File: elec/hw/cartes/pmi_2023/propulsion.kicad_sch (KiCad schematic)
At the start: 45 parts, among them Q1 SI2310, U1 DRV8231ADDAR, U2 DRV8231ADDAR, U3 EESX1321, U4 EESX1321

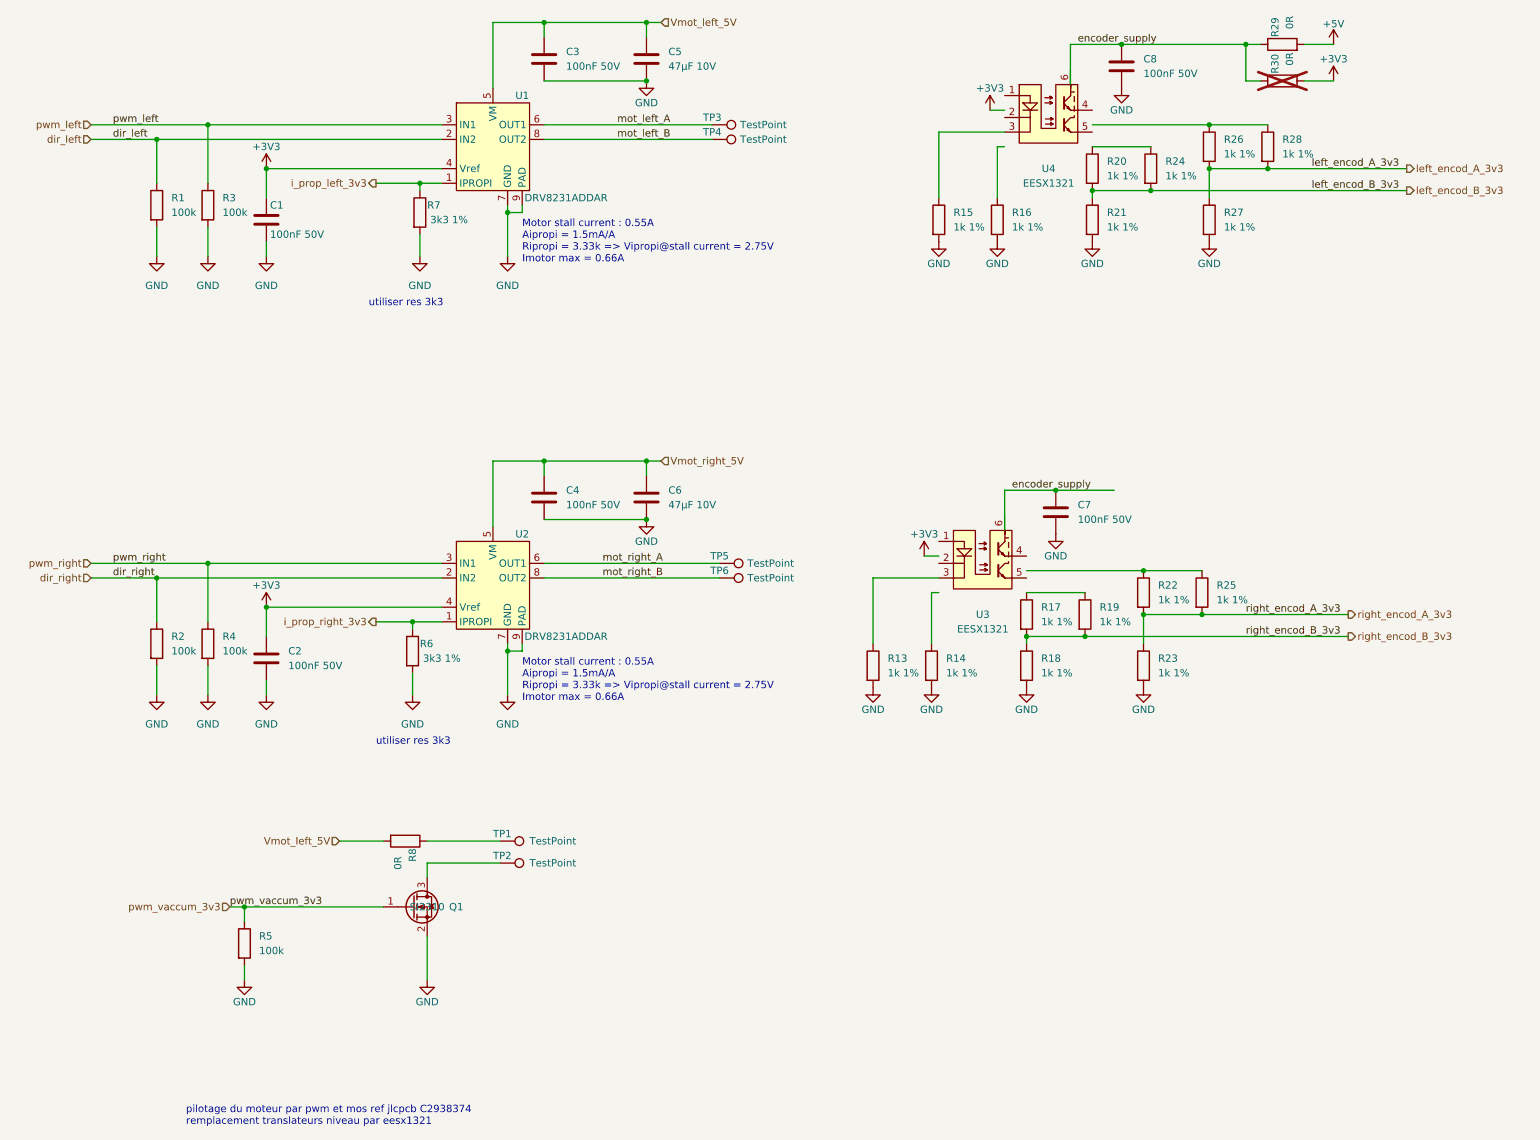
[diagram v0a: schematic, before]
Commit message: reset button added to esp32 reset. uart prog connector replaces ftdi one
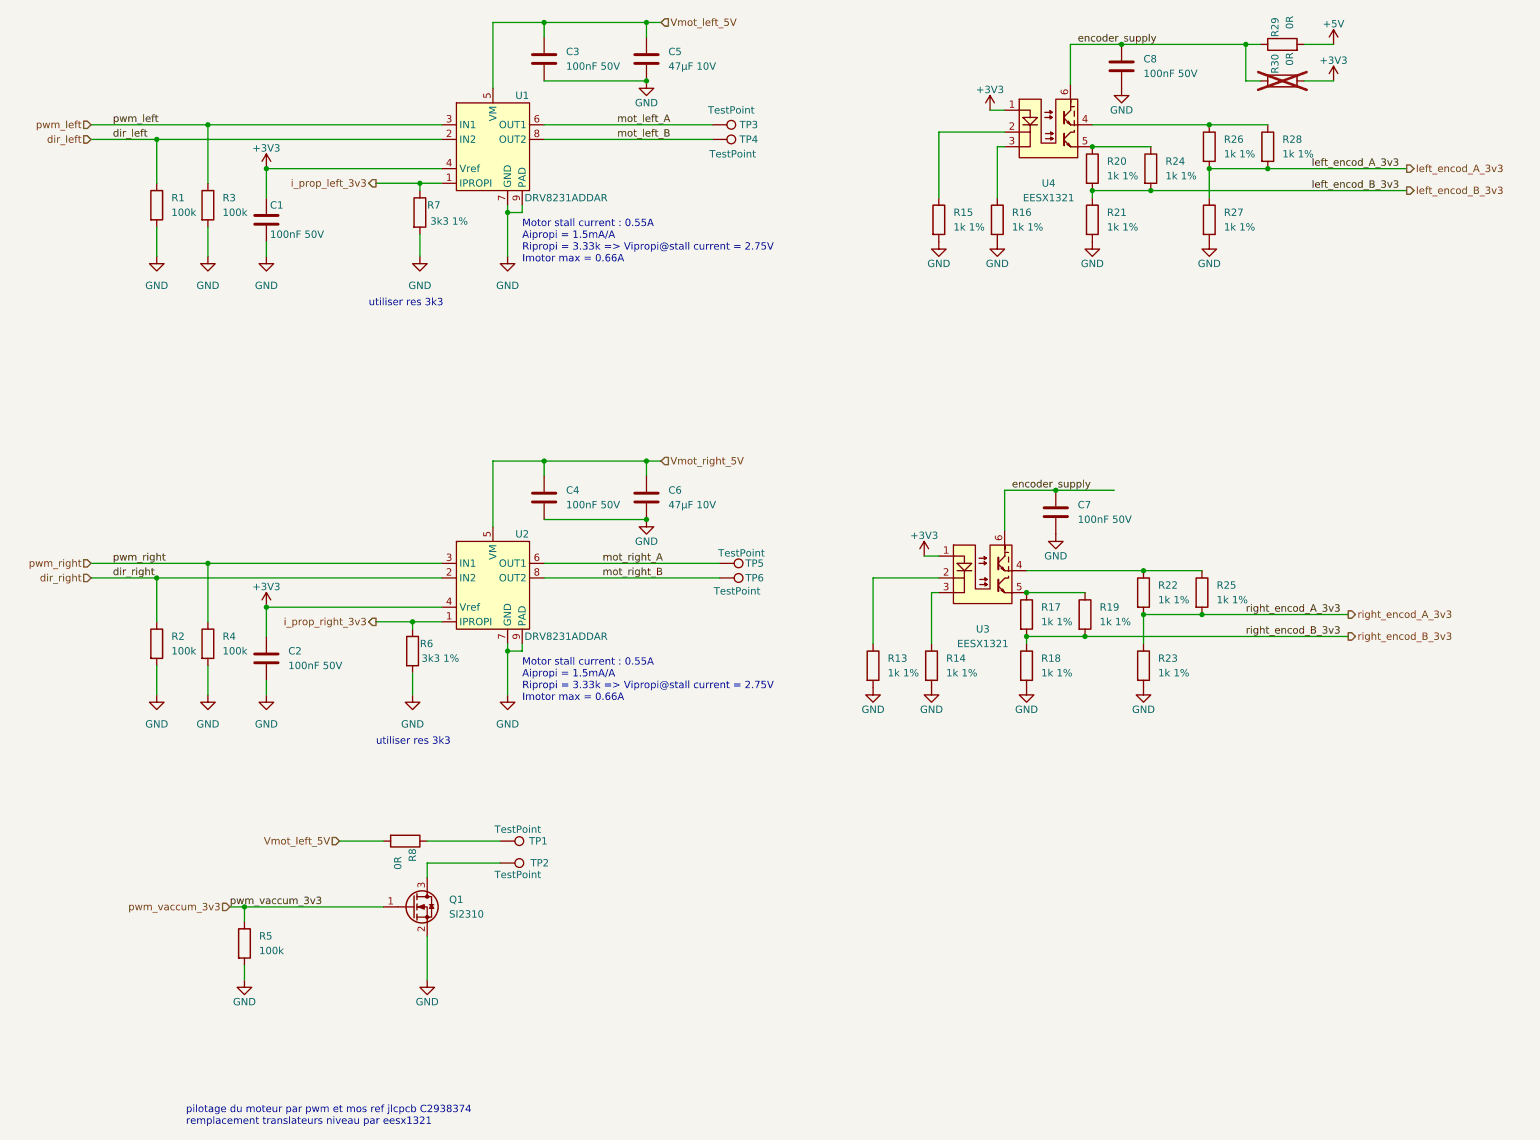
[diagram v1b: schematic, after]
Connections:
- net +3V3: now also U3.1 (A), U4.1 (A)
- net encoder_supply: now also U3.6 (C), U4.6 (C)
- net at R14.1: now also U3.3 (C2)
- net at R22.1, R25.1: now also U3.4 (E1)
- net at R17.1, R19.1: now also U3.5 (E2)
- net at R26.1, R28.1: now also U4.4 (E1)
- net at R20.1, R24.1: now also U4.5 (E2)
- net at U3.2 (C1): now also R13.1
- net at U4.2 (C1): now also R15.1
- net at U4.3 (C2): now also R16.1; no longer R15.1
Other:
- moved on the sheet: U3, U4

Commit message: PAMI 2023: update jlc part number
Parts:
- R13, R14, R15, R16, R17, R18, R19, R20, R21, R22, R23, R24, R25, R26, R27, R28: JLCPCB C2991540 -> C21190
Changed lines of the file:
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@@
 			)
 		)
-		(property "JLCPCB" "C2991540"
+		(property "JLCPCB" "C21190"
 			(at 171.45 135.89 0)
 			(effects
@@
 			)
 		)
-		(property "JLCPCB" "C2991540"
+		(property "JLCPCB" "C21190"
 			(at 218.44 123.19 0)
 			(effects
@@
 			)
 		)
-		(property "JLCPCB" "C2991540"
+		(property "JLCPCB" "C21190"
 			(at 187.96 127 0)
 			(effects
@@
 			)
 		)
-		(property "JLCPCB" "C2991540"
+		(property "JLCPCB" "C21190"
 			(at 198.12 127 0)
 			(effects
@@
 			)
 		)
-		(property "JLCPCB" "C2991540"
+		(property "JLCPCB" "C21190"
 			(at 219.71 45.72 0)
 			(effects
@@
 			)
 		)
-		(property "JLCPCB" "C2991540"
+		(property "JLCPCB" "C21190"
 			(at 199.39 49.53 0)
 			(effects
@@
 			)
 		)
-		(property "JLCPCB" "C2991540"
+		(property "JLCPCB" "C21190"
 			(at 209.55 49.53 0)
 			(effects
@@
 			)
 		)
-		(property "JLCPCB" "C2991540"
+		(property "JLCPCB" "C21190"
 			(at 219.71 58.42 0)
 			(effects
@@
 			)
 		)
-		(property "JLCPCB" "C2991540"
+		(property "JLCPCB" "C21190"
 			(at 208.28 135.89 0)
 			(effects
@@
 			)
 		)
-		(property "JLCPCB" "C2991540"
+		(property "JLCPCB" "C21190"
 			(at 229.87 45.72 0)
 			(effects
@@
 			)
 		)
-		(property "JLCPCB" "C2991540"
+		(property "JLCPCB" "C21190"
 			(at 161.29 135.89 0)
 			(effects
@@
 			)
 		)
-		(property "JLCPCB" "C2991540"
+		(property "JLCPCB" "C21190"
 			(at 208.28 123.19 0)
 			(effects
@@
 			)
 		)
-		(property "JLCPCB" "C2991540"
+		(property "JLCPCB" "C21190"
 			(at 182.88 58.42 0)
 			(effects
@@
 			)
 		)
-		(property "JLCPCB" "C2991540"
+		(property "JLCPCB" "C21190"
 			(at 187.96 135.89 0)
 			(effects
@@
 			)
 		)
-		(property "JLCPCB" "C2991540"
+		(property "JLCPCB" "C21190"
 			(at 199.39 58.42 0)
 			(effects
@@
 			)
 		)
-		(property "JLCPCB" "C2991540"
+		(property "JLCPCB" "C21190"
 			(at 172.72 58.42 0)
 			(effects

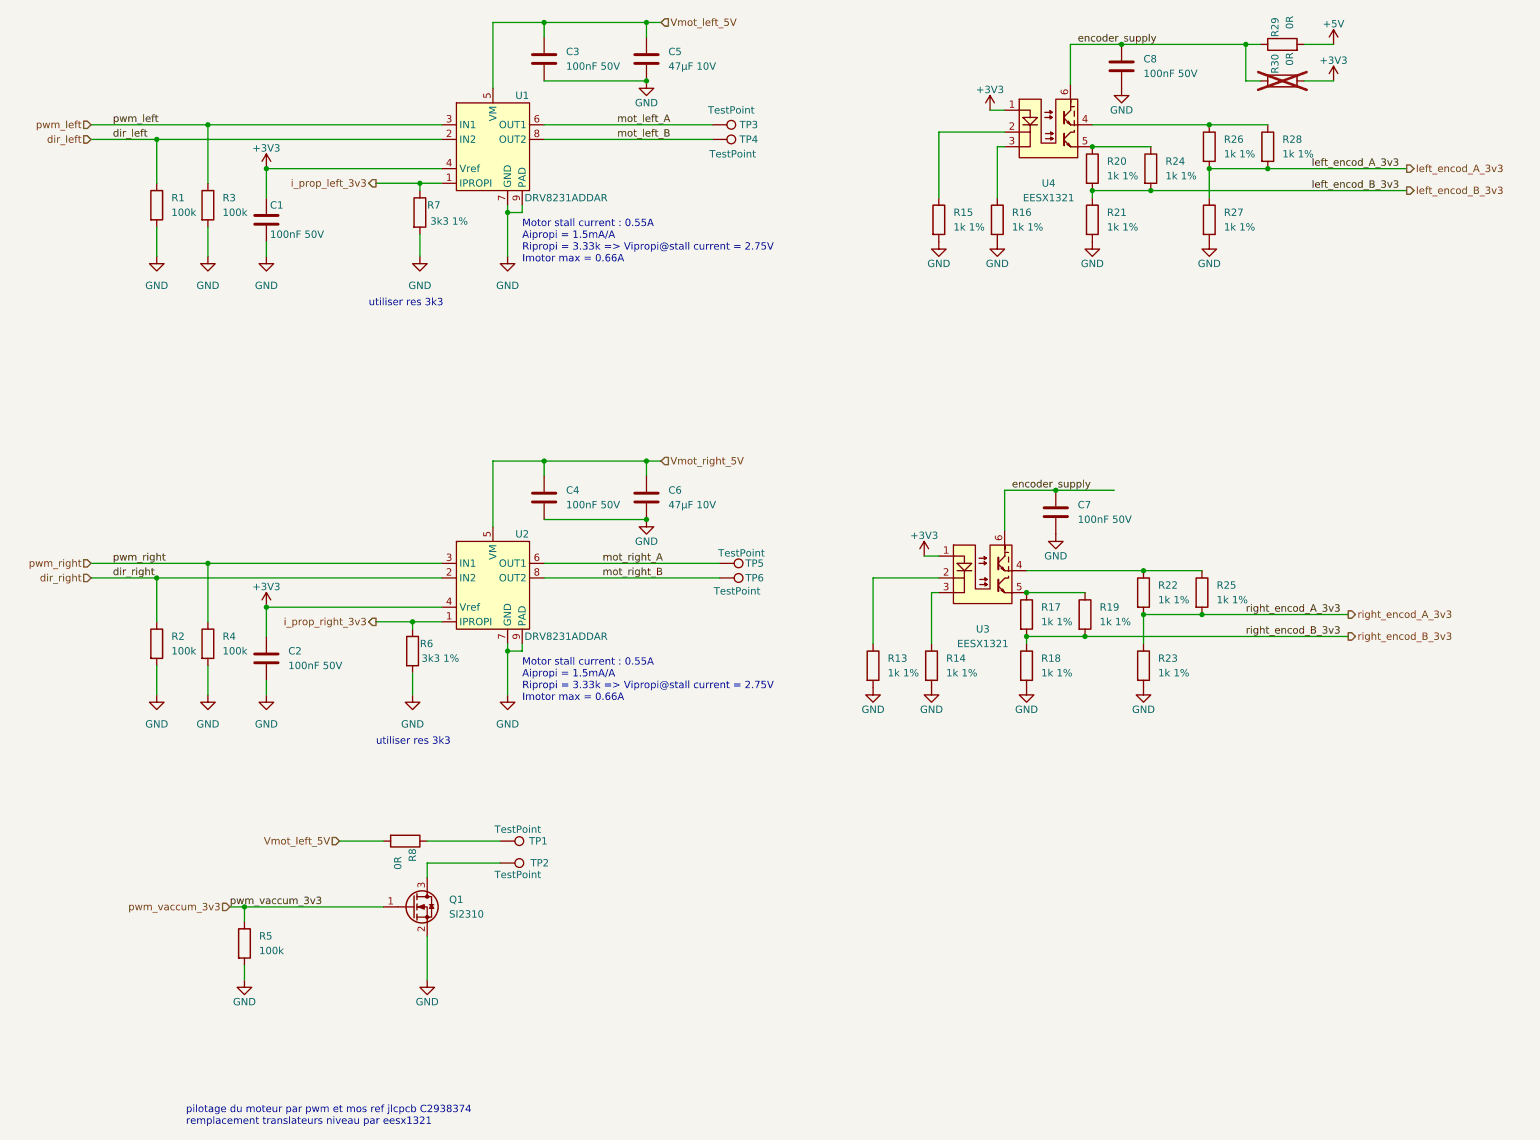
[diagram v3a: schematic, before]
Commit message: pmi_tof_sensor : last commit before tmf8821 deletion
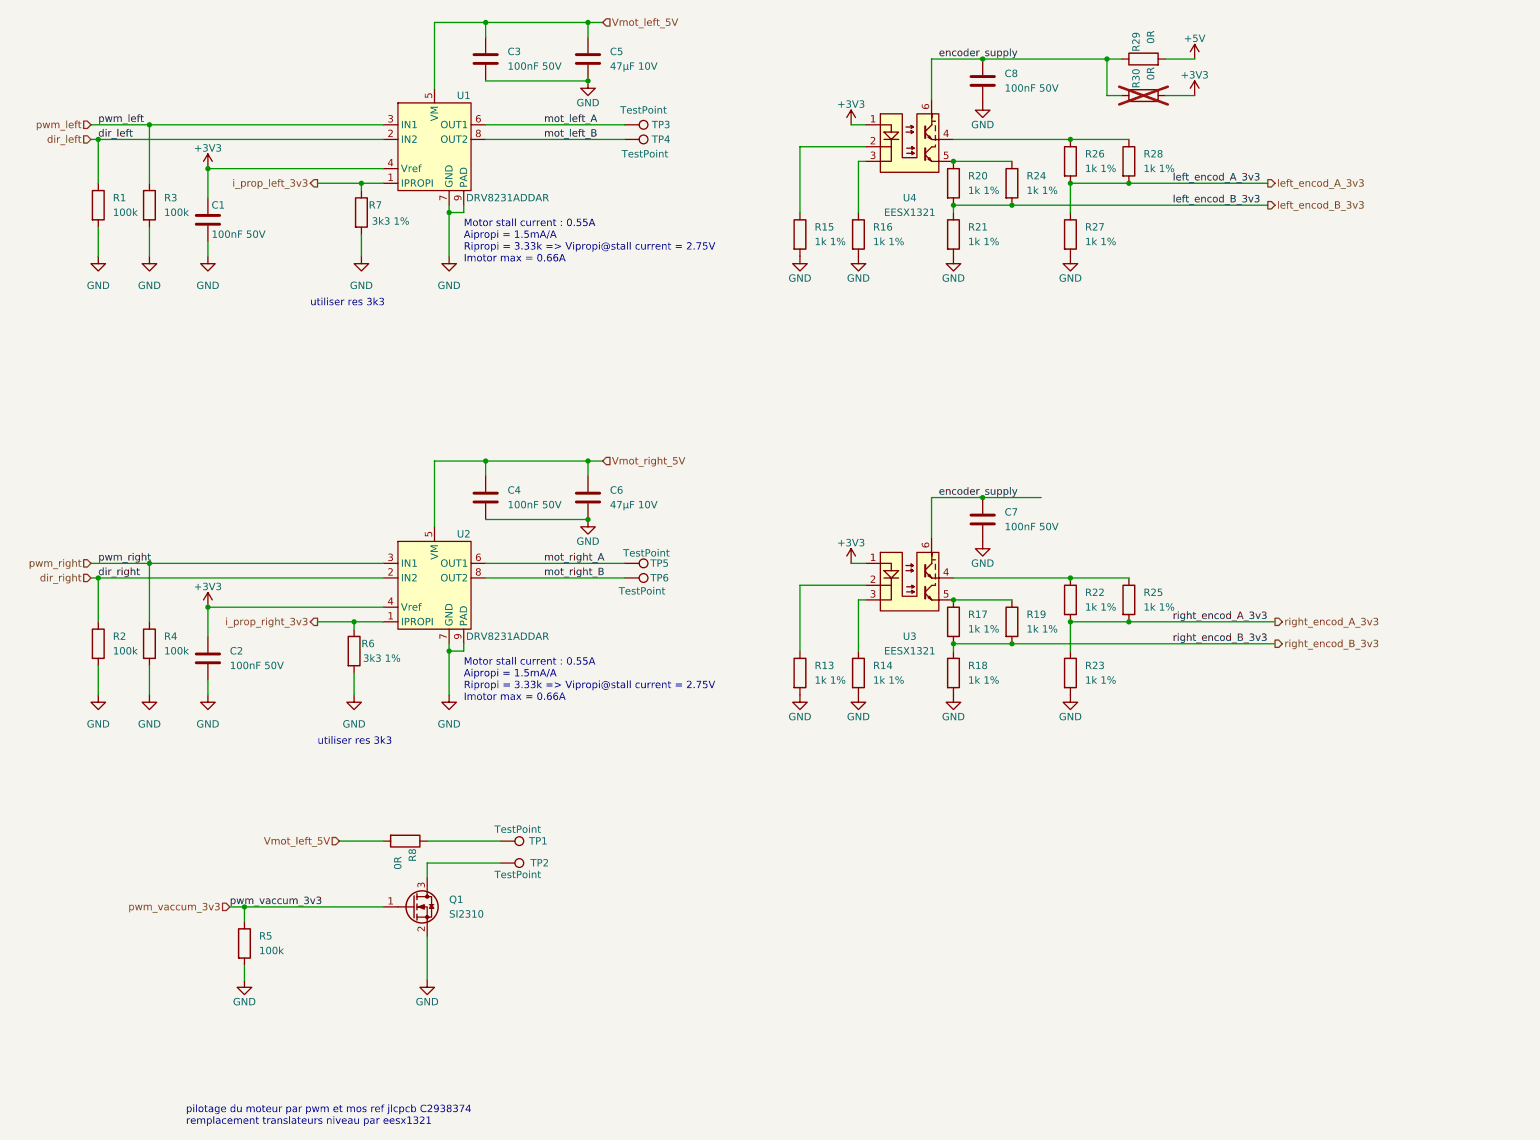
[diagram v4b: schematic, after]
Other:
- moved on the sheet: C1, C2, C3, C4, C5, C6, C7, C8, R1, R13, R14, R15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

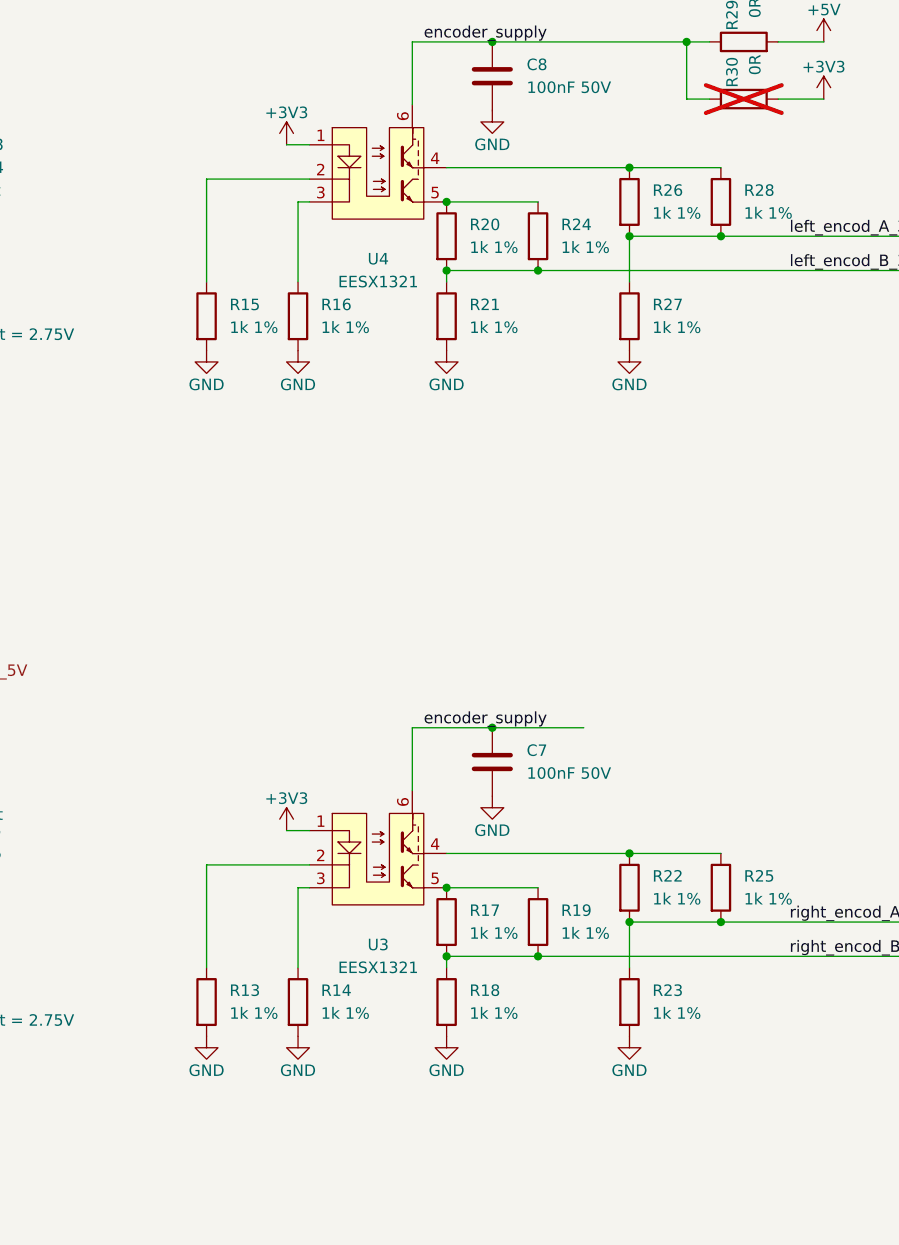
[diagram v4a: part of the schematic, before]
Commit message: encoder resistors values corrected
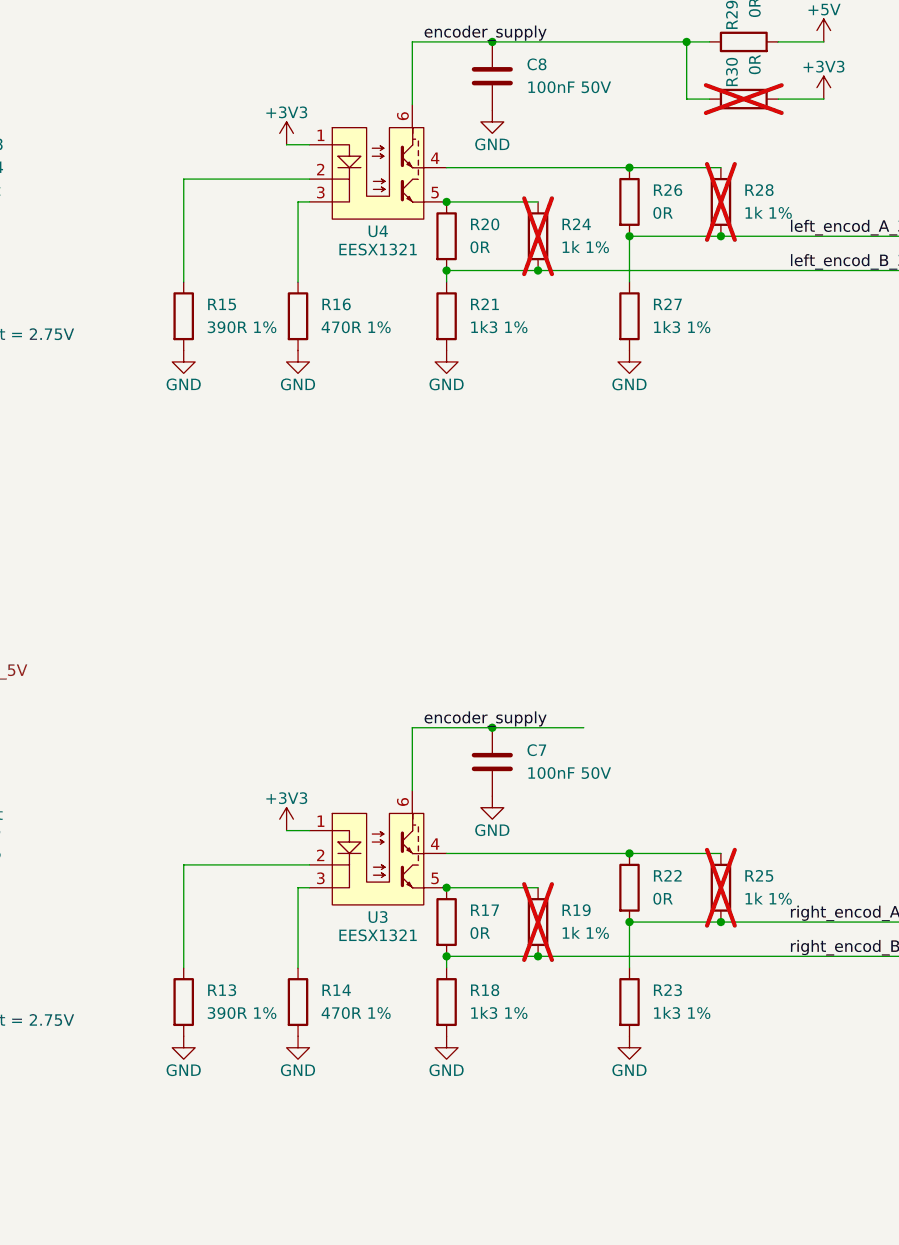
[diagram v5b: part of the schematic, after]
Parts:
- R13, R15: value 1k 1% -> 390R 1%; symbol cocotter_resistors:R_1k_0603_1% -> cocotter_resistors:R_390R_0603_1%; JLCPCB C21190 -> C23151; Specification 10k 0603 1% 100mW -> 390R 0603 1% 100mW; mouser 603-RC0603FR-10100KL -> (none)
- R14, R16: value 1k 1% -> 470R 1%; symbol cocotter_resistors:R_1k_0603_1% -> cocotter_resistors:R_470R_0603_1%; JLCPCB C21190 -> C23179; Specification 10k 0603 1% 100mW -> 470R 0603 1% 100mW; mouser 603-RC0603FR-10100KL -> (none)
- R17, R20, R22, R26: value 1k 1% -> 0R; symbol cocotter_resistors:R_1k_0603_1% -> cocotter_resistors:R_0R_0603; JLCPCB C21190 -> C431718; Specification 10k 0603 1% 100mW -> 0R 0603 20mOhms max 100mW; mouser 603-RC0603FR-10100KL -> (none)
- R18, R21, R23, R27: value 1k 1% -> 1k3 1%; symbol cocotter_resistors:R_1k_0603_1% -> cocotter_resistors:R_1k3_0603_1%; JLCPCB C21190 -> C22767; Specification 10k 0603 1% 100mW -> 1k3 0603 1% 100mW; mouser 603-RC0603FR-10100KL -> (none)
- R19, R24, R25, R28: now not fitted
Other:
- moved on the sheet: R13, R15
